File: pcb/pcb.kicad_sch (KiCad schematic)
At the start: 54 parts, among them K00 Kailh Choc, K01 Kailh Choc, K02 Kailh Choc, K03 Kailh Choc, K10 Kailh Choc, K11 Kailh Choc, K12 Kailh Choc, K13 Kailh Choc, K20 Kailh Choc, K21 Kailh Choc, K22 Kailh Choc, K23 Kailh Choc, K30 Kailh Choc, K31 Kailh Choc, K32 Kailh Choc, K33 Kailh Choc, K40 Kailh Choc, K41 Kailh Choc, K42 Kailh Choc, K43 Kailh Choc, K50 Kailh Choc, K51 Kailh Choc, K52 Kailh Choc, K53 Kailh Choc, K60 Kailh Choc, K61 Kailh Choc, SW1 SW_DPST, U1 nice_nano

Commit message: first pass at pcb and case
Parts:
- removed D00, D01, D02, D03, D10, D11, D12, D13, D20, D21, D22, D23, D30, D31, D32, D33, D40, D41, D42, D43, D50, D51, D52, D53, D60, D61: 1N4148, Diode_THT:D_DO-35_SOD27_P7.62mm_Horizontal, symbol Diode:1N4148
- added J1: Screw_Terminal_01x02, Connector_JST:JST_PH_S2B-PH-K_1x02_P2.00mm_Horizontal, symbol Connector:Screw_Terminal_01x02
- SW1: symbol Switch:SW_DPST -> Switch:SW_Push
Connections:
- net Col0: now also U1.14 (NFC2/P0.10); no longer U1.20 (AIN7/P0.31)
- net Col1: now also U1.16 (P1.13); no longer U1.19 (AIN5/P0.29)
- net Col2: now also U1.15 (P1.11); no longer U1.18 (AIN0/P0.02)
- net Col4: now also U1.18 (AIN0/P0.02); no longer U1.16 (P1.13)
- net Col5: now also U1.19 (AIN5/P0.29); no longer U1.15 (P1.11)
- net Col6: now also U1.20 (AIN7/P0.31); no longer U1.14 (NFC2/P0.10)
- net GND: now also J1.2 (Pin_2); no longer SW1.3
- net Row0: now also K00.2 (B), K10.2 (B), K20.2 (B), K30.2 (B), K40.2 (B), K50.2 (B), K60.2 (B)
- net Row1: now also K01.2 (B), K11.2 (B), K21.2 (B), K31.2 (B), K41.2 (B), K51.2 (B), K61.2 (B)
- net Row2: now also K02.2 (B), K12.2 (B), K22.2 (B), K32.2 (B), K42.2 (B), K52.2 (B)
- net Row3: now also K03.2 (B), K13.2 (B), K23.2 (B), K33.2 (B), K43.2 (B), K53.2 (B)
- net at SW1.2, U1.22 (RST): no longer SW1.4
- net at U1.24 (BATIN/P0.04): now also J1.1 (Pin_1)
- no-connect marks 1 -> 4
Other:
- note added: "NOTE: Normally each switch would have a diode. This schematic omits the diodes because the switch footprints already include the diodes"

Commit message: refining the shape
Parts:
- removed K61: Kailh Choc, lib:Kailh_socket_PG1350_reversible, symbol Switch:SW_SPST
- added JP1, JP2, JP3, JP4: SolderJumper_2_Open, Jumper:SolderJumper-2_P1.3mm_Open_TrianglePad1.0x1.5mm, symbol Jumper:SolderJumper_2_Open
- added SW2: SW_SPDT, Button_Switch_SMD:SW_SPDT_CK-JS102011SAQN, symbol Switch:SW_SPDT
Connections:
- net Col0: now also U1.15 (P1.11); no longer U1.14 (NFC2/P0.10)
- net Col2: now also U1.17 (P1.15); no longer U1.15 (P1.11)
- net Col3: now also U1.18 (AIN0/P0.02); no longer U1.17 (P1.15)
- net Col4: now also U1.19 (AIN5/P0.29); no longer U1.18 (AIN0/P0.02)
- net Col5: now also U1.20 (AIN7/P0.31); no longer U1.19 (AIN5/P0.29)
- net Col6: now also U1.14 (NFC2/P0.10); no longer U1.20 (AIN7/P0.31)
- net GND: now also SW1.2, SW2.1 (A); no longer J1.2 (Pin_2), SW1.1
- net at U1.22 (RST): now also SW1.1; no longer SW1.2
- net at J1.1 (Pin_1): now also JP1.2 (B), JP2.2 (B); no longer U1.24 (BATIN/P0.04)
- new net: JP1.1 (A), JP3.1 (A), SW2.2 (B)
- new net: JP2.1 (A), JP4.1 (A), U1.24 (BATIN/P0.04)
- new net: J1.2 (Pin_2), JP3.2 (B), JP4.2 (B)
- no-connect marks 4 -> 5
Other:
- moved on the sheet: J1, SW1

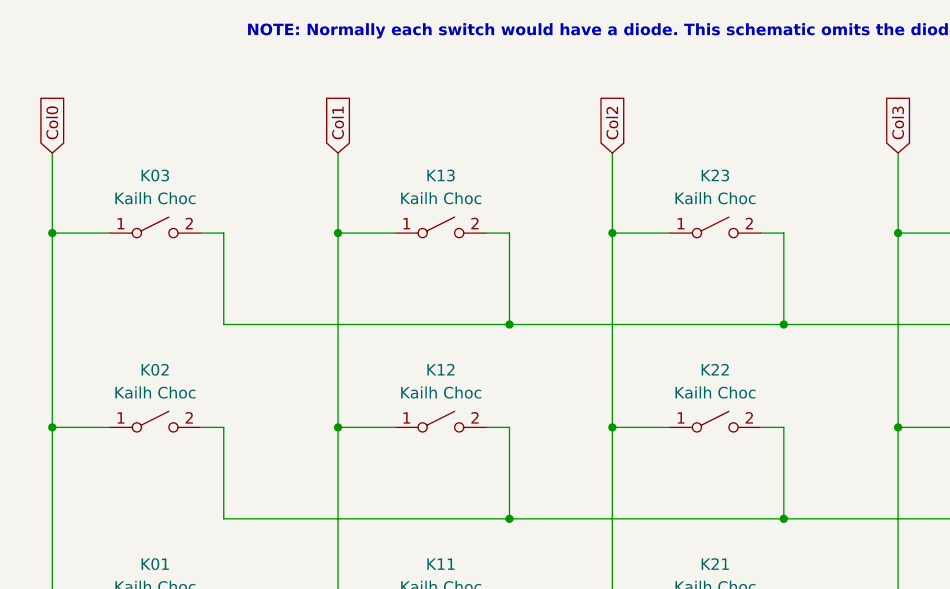
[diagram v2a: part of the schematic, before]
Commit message: update pcb for new shape
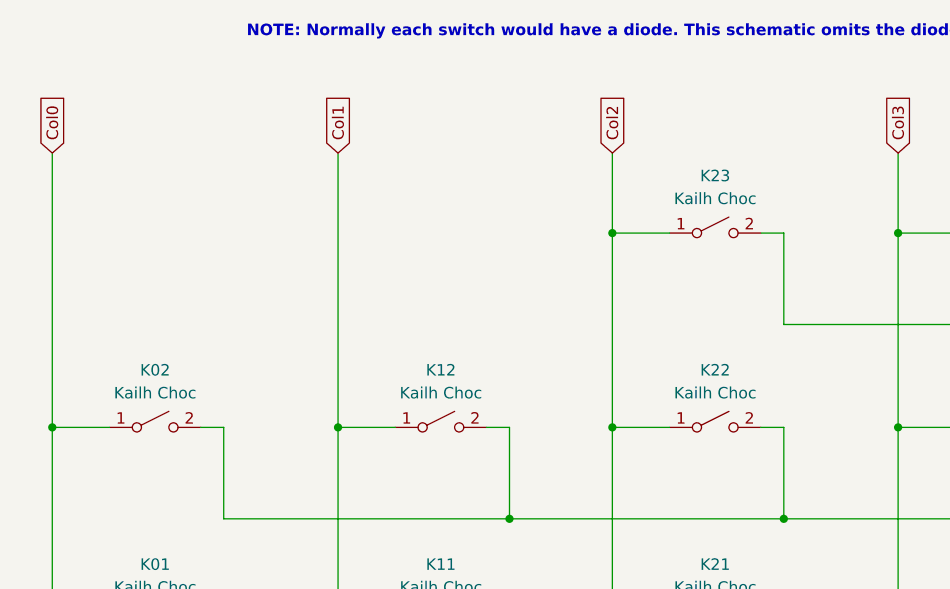
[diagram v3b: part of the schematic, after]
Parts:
- removed K03, K13: Kailh Choc, lib:Kailh_socket_PG1350_reversible, symbol Switch:SW_SPST
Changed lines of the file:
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@@
   (junction (at 220.98 49.53) (diameter 0) (color 0 0 0 0)
   )
-  (junction (at 77.47 39.37) (diameter 0) (color 0 0 0 0)
-  )
   (junction (at 167.64 127) (diameter 0) (color 0 0 0 0)
   )
@@
   (junction (at 170.18 39.37) (diameter 0) (color 0 0 0 0)
   )
-  (junction (at 127 49.53) (diameter 0) (color 0 0 0 0)
-  )
   (junction (at 77.47 60.96) (diameter 0) (color 0 0 0 0)
   )
@@
   (junction (at 45.72 82.55) (diameter 0) (color 0 0 0 0)
   )
-  (junction (at 96.52 49.53) (diameter 0) (color 0 0 0 0)
-  )
   (junction (at 107.95 39.37) (diameter 0) (color 0 0 0 0)
   )
@@
   )
   (junction (at 77.47 82.55) (diameter 0) (color 0 0 0 0)
-  )
-  (junction (at 45.72 39.37) (diameter 0) (color 0 0 0 0)
   )
   (junction (at 158.75 92.71) (diameter 0) (color 0 0 0 0)
@@
   (no_connect (at 71.12 186.69))
   (no_connect (at 67.31 186.69))
-  (wire (pts (xy 77.47 39.37) (xy 83.82 39.37))
-    (stroke (width 0) (type default) (color 0 0 0 0))
-  )
   (wire (pts (xy 237.49 30.48) (xy 237.49 104.14))
     (stroke (width 0) (type default) (color 0 0 0 0))
   )
-  (wire (pts (xy 45.72 30.48) (xy 45.72 39.37))
+  (wire (pts (xy 45.72 30.48) (xy 45.72 60.96))
     (stroke (width 0) (type default) (color 0 0 0 0))
   )
@@
     (stroke (width 0) (type default) (color 0 0 0 0))
   )
-  (wire (pts (xy 96.52 39.37) (xy 96.52 49.53))
-    (stroke (width 0) (type default) (color 0 0 0 0))
-  )
   (wire (pts (xy 53.34 153.67) (xy 57.15 153.67))
     (stroke (width 0) (type default) (color 0 0 0 0))
@@
     (stroke (width 0) (type default) (color 0 0 0 0))
   )
-  (wire (pts (xy 64.77 39.37) (xy 62.23 39.37))
-    (stroke (width 0) (type default) (color 0 0 0 0))
-  )
   (wire (pts (xy 252.73 104.14) (xy 252.73 114.3))
     (stroke (width 0) (type default) (color 0 0 0 0))
   )
-  (wire (pts (xy 45.72 39.37) (xy 52.07 39.37))
-    (stroke (width 0) (type default) (color 0 0 0 0))
-  )
   (wire (pts (xy 107.95 39.37) (xy 107.95 60.96))
     (stroke (width 0) (type default) (color 0 0 0 0))
@@
     (stroke (width 0) (type default) (color 0 0 0 0))
   )
-  (wire (pts (xy 77.47 39.37) (xy 77.47 60.96))
+  (wire (pts (xy 77.47 30.48) (xy 77.47 60.96))
     (stroke (width 0) (type default) (color 0 0 0 0))
   )
@@
     (stroke (width 0) (type default) (color 0 0 0 0))
   )
-  (wire (pts (xy 45.72 39.37) (xy 45.72 60.96))
-    (stroke (width 0) (type default) (color 0 0 0 0))
-  )
   (wire (pts (xy 127 92.71) (xy 158.75 92.71))
     (stroke (width 0) (type default) (color 0 0 0 0))
@@
     (stroke (width 0) (type default) (color 0 0 0 0))
   )
-  (wire (pts (xy 96.52 49.53) (xy 127 49.53))
-    (stroke (width 0) (type default) (color 0 0 0 0))
-  )
   (wire (pts (xy 220.98 82.55) (xy 220.98 92.71))
     (stroke (width 0) (type default) (color 0 0 0 0))
@@
     (stroke (width 0) (type default) (color 0 0 0 0))
   )
-  (wire (pts (xy 64.77 39.37) (xy 64.77 49.53))
-    (stroke (width 0) (type default) (color 0 0 0 0))
-  )
   (wire (pts (xy 96.52 129.54) (xy 96.52 148.59))
     (stroke (width 0) (type default) (color 0 0 0 0))
@@
     (stroke (width 0) (type default) (color 0 0 0 0))
   )
-  (wire (pts (xy 77.47 30.48) (xy 77.47 39.37))
-    (stroke (width 0) (type default) (color 0 0 0 0))
-  )
   (wire (pts (xy 158.75 49.53) (xy 189.23 49.53))
     (stroke (width 0) (type default) (color 0 0 0 0))
@@
     (stroke (width 0) (type default) (color 0 0 0 0))
   )
-  (wire (pts (xy 96.52 39.37) (xy 93.98 39.37))
-    (stroke (width 0) (type default) (color 0 0 0 0))
-  )
   (wire (pts (xy 96.52 71.12) (xy 127 71.12))
     (stroke (width 0) (type default) (color 0 0 0 0))
@@
   )
   (wire (pts (xy 237.49 104.14) (xy 240.03 104.14))
-    (stroke (width 0) (type default) (color 0 0 0 0))
-  )
-  (wire (pts (xy 64.77 49.53) (xy 96.52 49.53))
     (stroke (width 0) (type default) (color 0 0 0 0))
   )
@@
     )
   )
-  (symbol (lib_id "Switch:SW_SPST") (at 88.9 39.37 0) (unit 1)
-    (in_bom yes) (on_board yes) (fields_autoplaced)
-    (property "Reference" "K13" (id 0) (at 88.9 33.02 0))
-    (property "Value" "Kailh Choc" (id 1) (at 88.9 35.56 0))
-    (property "Footprint" "lib:Kailh_socket_PG1350_reversible" (id 2) (at 88.9 39.37 0)
-      (effects (font (size 1.27 1.27)) hide)
-    )
-    (property "Datasheet" "~" (id 3) (at 88.9 39.37 0)
-      (effects (font (size 1.27 1.27)) hide)
-    )
-    (pin "1")
-    (pin "2")
-  )
   (symbol (lib_id "Switch:SW_SPST") (at 151.13 104.14 0) (unit 1)
     (in_bom yes) (on_board yes) (fields_autoplaced)
@@
     )
     (property "Datasheet" "~" (id 3) (at 119.38 104.14 0)
-      (effects (font (size 1.27 1.27)) hide)
-    )
-    (pin "1")
-    (pin "2")
-  )
-  (symbol (lib_id "Switch:SW_SPST") (at 57.15 39.37 0) (unit 1)
-    (in_bom yes) (on_board yes) (fields_autoplaced)
-    (property "Reference" "K03" (id 0) (at 57.15 33.02 0))
-    (property "Value" "Kailh Choc" (id 1) (at 57.15 35.56 0))
-    (property "Footprint" "lib:Kailh_socket_PG1350_reversible" (id 2) (at 57.15 39.37 0)
-      (effects (font (size 1.27 1.27)) hide)
-    )
-    (property "Datasheet" "~" (id 3) (at 57.15 39.37 0)
       (effects (font (size 1.27 1.27)) hide)
     )
@@
       (reference "K02") (unit 1) (value "Kailh Choc") (footprint "lib:Kailh_socket_PG1350_reversible")
     )
-    (path "/340af0d1-9e76-4971-a8a5-118d879d0316"
-      (reference "K03") (unit 1) (value "Kailh Choc") (footprint "lib:Kailh_socket_PG1350_reversible")
-    )
     (path "/d0ec2905-f0e5-4489-b710-ebfec8cd3094"
       (reference "K10") (unit 1) (value "Kailh Choc") (footprint "lib:Kailh_socket_PG1350_reversible")
@@
       (reference "K12") (unit 1) (value "Kailh Choc") (footprint "lib:Kailh_socket_PG1350_reversible")
     )
-    (path "/00685ae2-2e2b-4657-a1a2-617216e0d961"
-      (reference "K13") (unit 1) (value "Kailh Choc") (footprint "lib:Kailh_socket_PG1350_reversible")
-    )
     (path "/310a27be-068a-4e18-9944-9d7f5baf3d72"

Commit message: update pcb
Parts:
- removed SW2: SW_SPDT, Button_Switch_SMD:SW_SPDT_CK-JS102011SAQN, symbol Switch:SW_SPDT
- added SW2, SW3: SW_Push_DPDT, lib:SW_JS202011SCQN (Reverse Mount), symbol Switch:SW_Push_DPDT
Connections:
- net GND: now also SW2.6 (C), SW3.4 (A)
- net at JP1.1 (A), JP3.1 (A): now also SW2.5 (B), SW3.5 (B)
- net at JP2.1 (A), JP4.1 (A): now also SW2.2 (B), SW3.2 (B); no longer U1.24 (BATIN/P0.04)
- new net: SW2.3 (C), SW3.1 (A), U1.24 (BATIN/P0.04)
- no-connect marks 5 -> 8
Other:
- moved on the sheet: J1, JP1, JP2, JP3, JP4, SW1, U1

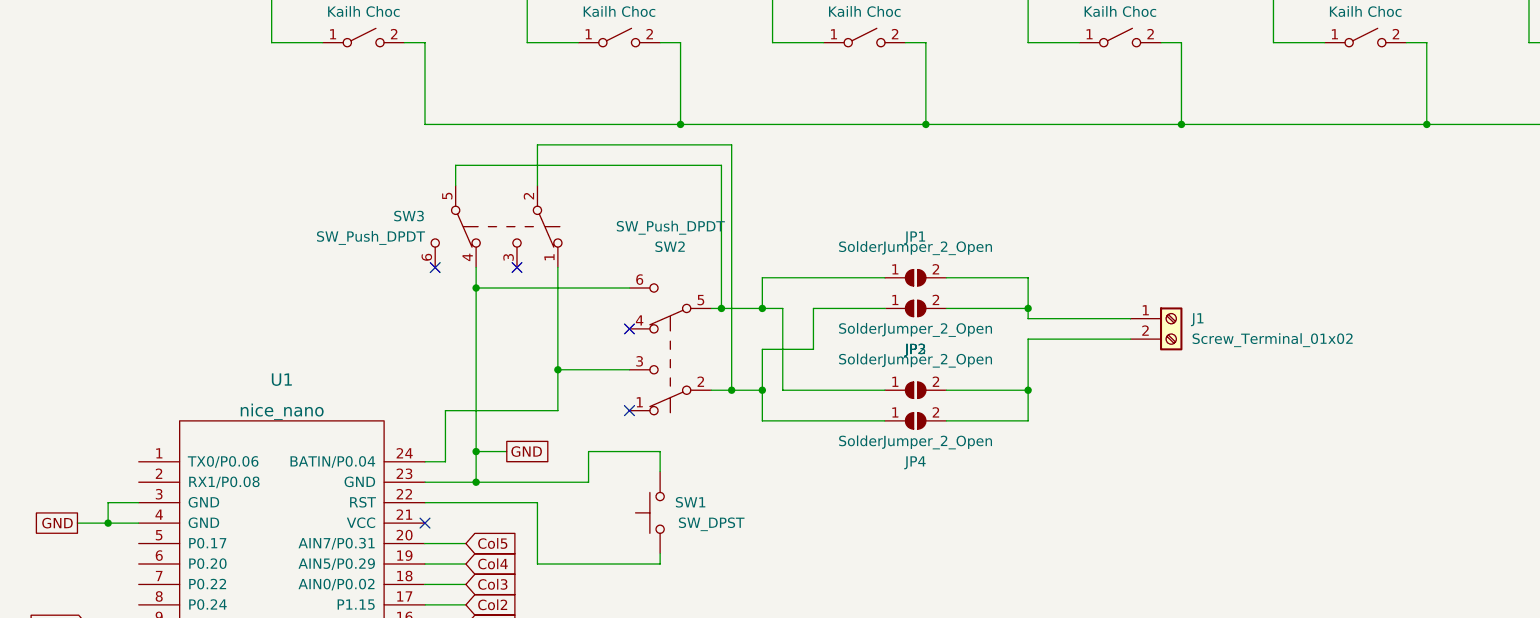
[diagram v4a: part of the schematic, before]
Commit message: switch to low-profile battery connector
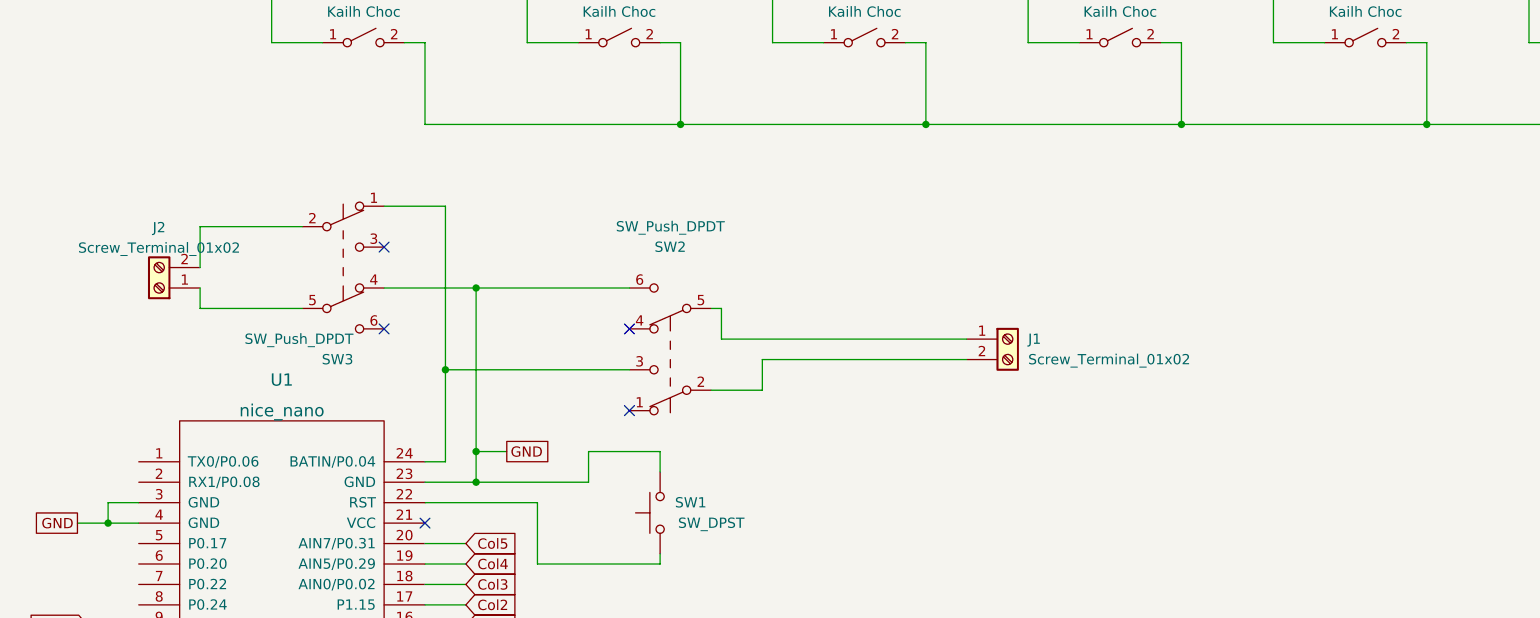
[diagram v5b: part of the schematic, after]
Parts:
- removed JP1, JP2, JP3, JP4: SolderJumper_2_Open, Jumper:SolderJumper-2_P1.3mm_Open_TrianglePad1.0x1.5mm, symbol Jumper:SolderJumper_2_Open
- added J2: Screw_Terminal_01x02, lib:BM02B-ACHSS-GAN-ETF, symbol Connector:Screw_Terminal_01x02
- J1: footprint Connector_JST:JST_PH_S2B-PH-K_1x02_P2.00mm_Horizontal -> lib:BM02B-ACHSS-GAN-ETF
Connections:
- net at SW3.2 (B): now also J2.2 (Pin_2); no longer SW2.2 (B)
- net at SW3.5 (B): now also J2.1 (Pin_1); no longer SW2.5 (B)
- net at J1.1 (Pin_1): now also SW2.5 (B)
- net at J1.2 (Pin_2): now also SW2.2 (B)
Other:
- moved on the sheet: J1, SW3

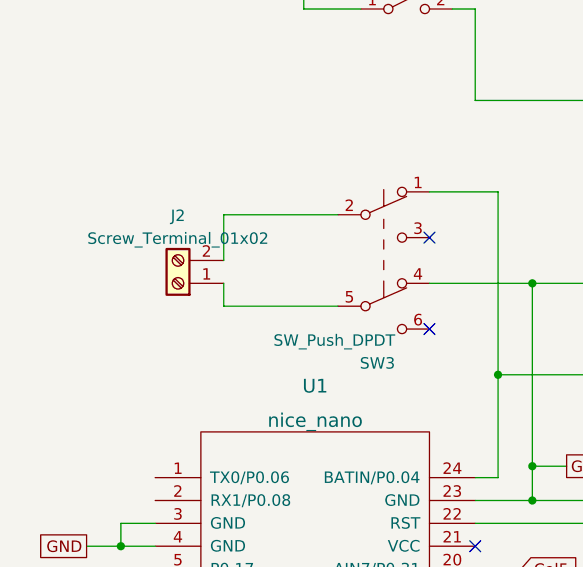
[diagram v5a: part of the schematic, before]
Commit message: update pcb for low pro battery connector
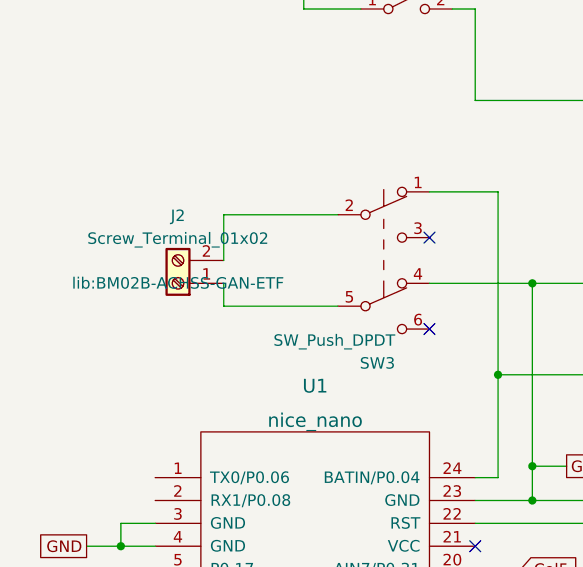
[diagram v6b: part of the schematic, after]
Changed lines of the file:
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@@
     (property "Reference" "J2" (id 0) (at 31.75 127.1102 0))
     (property "Value" "Screw_Terminal_01x02" (id 1) (at 31.75 129.6471 0))
-    (property "Footprint" "lib:BM02B-ACHSS-GAN-ETF" (id 2) (at 31.75 134.62 0)
-      (effects (font (size 1.27 1.27)) hide)
-    )
+    (property "Footprint" "lib:BM02B-ACHSS-GAN-ETF" (id 2) (at 31.75 134.62 0))
     (property "Datasheet" "https://www.jst-mfg.com/product/pdf/eng/ePH.pdf" (id 3) (at 31.75 134.62 0)
       (effects (font (size 1.27 1.27)) hide)
